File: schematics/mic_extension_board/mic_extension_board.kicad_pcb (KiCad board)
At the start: 2 copper layers, 87 x 62.2 mm, 126 parts, among them J1 XLR3, J12 Conn_01x01_Female, J13 Conn_01x01_Female, J2 Conn_01x02_Male, J3 Aux In, J4 Conn_01x02_Pin, J5 6Pin ISP, J7 XLR3, J8 XLR3, J9 Conn_01x03_Female, SW1 Stompbutton 1, SW2 Stompbutton 2, SW3 Stompbutton 3, U1 TL074, U10 LM4881M/NOPB, U11 CS4270-CZZ, U2 TL072, U3 k7833, U4 NE5534, U5 ATmega88A-A, U6 24LC128, U7 MC78M09_TO252, U8 MC78M05_TO252, U9 TL072, X1 SG-5032CAN

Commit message: finished full board
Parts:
- added C38: C, Capacitor_SMD:C_0805_2012Metric_Pad1.18x1.45mm_HandSolder, F.Cu at (187.9, 84.0)
- added C39: C, Capacitor_SMD:C_0805_2012Metric_Pad1.18x1.45mm_HandSolder, F.Cu at (187.9, 89.0)
- added D1: LED, Connector_PinHeader_2.54mm:PinHeader_1x02_P2.54mm_Vertical, F.Cu at (155.5, 124.6)
- added D8: LED, Connector_PinHeader_2.54mm:PinHeader_1x02_P2.54mm_Vertical, F.Cu at (151.0, 124.6)
- added J6: Conn_01x03_Female, Connector_PinHeader_2.54mm:PinHeader_1x03_P2.54mm_Vertical, F.Cu at (159.9, 66.2)
- added R50: R, Resistor_SMD:R_0603_1608Metric_Pad0.98x0.95mm_HandSolder, F.Cu at (194.8, 84.0)
- added R51: R, Resistor_SMD:R_0603_1608Metric_Pad0.98x0.95mm_HandSolder, F.Cu at (191.7, 84.0)
- added R52: R, Resistor_SMD:R_0603_1608Metric_Pad0.98x0.95mm_HandSolder, F.Cu at (194.8, 89.0)
- added R53: R, Resistor_SMD:R_0603_1608Metric_Pad0.98x0.95mm_HandSolder, F.Cu at (191.7, 89.0)
- added R54: 180, Resistor_SMD:R_0603_1608Metric_Pad0.98x0.95mm_HandSolder, F.Cu at (158.7, 125.9)
- added R55: 180, Resistor_SMD:R_0603_1608Metric_Pad0.98x0.95mm_HandSolder, F.Cu at (147.9, 125.9)
- added RV3: 25k, Connector_PinHeader_2.54mm:PinHeader_1x03_P2.54mm_Vertical, F.Cu at (175.8, 128.4)
- added RV4: 25k, Connector_PinHeader_2.54mm:PinHeader_1x03_P2.54mm_Vertical, F.Cu at (180.9, 128.4)
- added RV5: 25k, Connector_PinHeader_2.54mm:PinHeader_1x03_P2.54mm_Vertical, F.Cu at (185.3, 128.4)
- added SW4: Enter, Connector_PinHeader_2.54mm:PinHeader_1x02_P2.54mm_Vertical, F.Cu at (170.1, 124.6)
- added SW5: Exit, Connector_PinHeader_2.54mm:PinHeader_1x02_P2.54mm_Vertical, F.Cu at (163.1, 124.6)
- added U12: 128X64 OLED Display, Connector_PinHeader_2.54mm:PinHeader_1x07_P2.54mm_Vertical, F.Cu at (140.2, 132.2)
- added U13: Debug Port, Connector_PinHeader_2.54mm:PinHeader_1x06_P2.54mm_Vertical, F.Cu at (182.2, 132.8)
- C1: value 33pF -> C; footprint Capacitor_SMD:C_0603_1608Metric_Pad1.08x0.95mm_HandSolder -> Capacitor_SMD:C_0805_2012Metric_Pad1.18x1.45mm_HandSolder
- C10, C21, C22: value 4.7uF -> C_Polarized
- C11, C12: value 330uF -> C_Polarized
- C13, C15, C17, C23, C25, C3, C33: value 10uF -> C_Polarized
- C14, C5, C6: value 22uF -> C_Polarized
- C16, C24, C26, C31, C34, C35: value 0.1uF -> C
- C18, C27, C28: value 220pF -> C
- C19, C2, C20, C7, C8, C9: value 1uF -> C_Polarized
- C29, C30: value 3.3uF -> C_Polarized
- C32: value 47uF -> C_Polarized
- C36, C37: value 3.3nF -> C
- C4: value 47pF -> C
- J5: value 6Pin ISP -> Conn_02x03_Odd_Even
- J9: value Conn_01x03_Female -> Conn_01x03
- L1: value 22uH -> L
- R1, R15, R16, R18, R2, R29, R3, R4: value 22k -> R
- R10, R17, R19, R21, R22, R24, R25, R26, R27, R28, R31, R34, R35, R46, R47, R9: value 10k -> R
- R11, R12, R13, R14, R7, R8: value 180 -> R
- R20, R23, R42, R5: value 4k7 -> R
- R30, R32, R33, R6: value 150 -> R
- R36, R37, R38, R39: value 12k -> R
- R40: value 1M -> R
- R41, R44, R45: value 2k2 -> R
- R43: value 47k -> R
- R48, R49: value 470 -> R
- RV1: value 100k -> R_Potentiometer
- RV2: value 10k -> R_Potentiometer
- SW1: value Stompbutton 1 -> SW_Push
- SW2: value Stompbutton 2 -> SW_Push
- SW3: value Stompbutton 3 -> SW_Push
- U2: value TL072 -> Pico; footprint Package_SO:SOIC-8_3.9x4.9mm_P1.27mm -> MCU_RaspberryPi_and_Boards:RPi_Pico_SMD_TH
- U3: value k7833 -> LM7809_TO220; footprint Connector_PinHeader_2.54mm:PinHeader_1x03_P2.54mm_Vertical -> Package_TO_SOT_THT:TO-220-3_Vertical
- U7: value MC78M09_TO252 -> MC78M05_TO252
- U9: value TL072 -> TL074; footprint Package_SO:SOIC-8_3.9x4.9mm_P1.27mm -> Package_SO:SOIC-14_3.9x8.7mm_P1.27mm
- moved U2 106.4 mm to (175.2, 106.2), turned to -90 degrees
- moved J9 104.6 mm to (198.0, 88.4), turned to 180 degrees
- moved H1 94.0 mm to (196.8, 131.6)
- moved R45 84.0 mm to (87.9, 105.7), turned to 180 degrees
- moved J7 81.5 mm to (140.2, 66.2), turned to -90 degrees
- moved C25 81.2 mm to (112.3, 74.4), turned to 90 degrees
- moved R27 79.8 mm to (132.0, 88.4)
- moved R30 79.5 mm to (139.2, 68.7), turned to 180 degrees
- moved R26 78.9 mm to (131.3, 82.0)
- moved R43 78.6 mm to (112.4, 84.3), turned to 180 degrees
- moved R44 78.4 mm to (88.7, 108.7), turned to 180 degrees
- moved C23 78.3 mm to (107.9, 90.3), turned to 90 degrees
- moved R18 77.9 mm to (146.3, 80.8)
- moved J13 77.6 mm to (110.9, 95.0)
- moved R19 77.1 mm to (135.4, 85.9)
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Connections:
- C11 pad 2: Net-(J9-Pin_2) -> Net-(J6-Pin_2)
- C12 pad 2: Net-(J9-Pin_3) -> Net-(J6-Pin_3)
- C16 pad 1: Net-(U1B-+) -> Net-(U1D-+)
- C18 pad 1: Net-(U9B--) -> Net-(U1B--)
- C19 pad 1: Net-(U9B-+) -> Net-(U1B-+)
- C24 pad 1: Net-(U11-VD) -> 3V3
- C26 pad 1: Net-(U11-VD) -> 3V3
- C8 pad 1: Net-(U9A-+) -> Net-(C8-Pad1)
- J9 pad 1: GND -> Net-(J9-Pin_1)
- J9 pad 2: Net-(J9-Pin_2) -> GND
- R19 pad 2: Net-(U1D--) -> Net-(U9D--)
- R20 pad 2: Net-(U1D--) -> Net-(U9D--)
- R21 pad 2: Net-(U1C--) -> Net-(U9C--)
- R22 pad 2: Net-(U2A--) -> Net-(U9A--)
- R23 pad 2: Net-(U2A--) -> Net-(U9A--)
- R24 pad 1: Net-(U2A--) -> Net-(U9A--)
- R25 pad 2: Net-(U2B--) -> Net-(U9B--)
- R26 pad 1: Net-(U1D--) -> Net-(U9D--)
- R27 pad 1: Net-(U1C--) -> Net-(U9C--)
- R28 pad 1: Net-(U2B--) -> Net-(U9B--)
- R36 pad 2: Net-(U1B-+) -> Net-(U1D-+)
- R37 pad 1: Net-(U1B-+) -> Net-(U1D-+)
- R38 pad 2: Net-(U9A-+) -> Net-(C8-Pad1)
- R39 pad 1: Net-(U9A-+) -> Net-(C8-Pad1)
- R40 pad 1: Net-(U9A--) -> Net-(C8-Pad1)
- R40 pad 2: Net-(U9B-+) -> Net-(U1B-+)
- R41 pad 1: Net-(U9B--) -> Net-(U1B--)
- R42 pad 1: Net-(U9B--) -> Net-(U1B--)
- R44 pad 2: Net-(U11-VD) -> 3V3
- R45 pad 2: Net-(U11-VD) -> 3V3
- U1 pad 10: VGND -> GND
- U1 pad 12: VGND -> Net-(U1D-+)
- U1 pad 13: Net-(U1D--) -> VGND
- U1 pad 14: Net-(C3-Pad1) -> VGND
- U1 pad 6: VGND -> Net-(U1B--)
- U1 pad 7: VGND -> Net-(C18-Pad2)
- U1 pad 8: Net-(C13-Pad1) -> Net-(U1C--)
- U11 pad 5: Net-(U11-VD) -> 3V3
- U11 pad 8: Net-(U11-VD) -> 3V3
- U2 pad 1: /Analog Preamp/Left Analog Out -> Net-(U13-UartTX)
- U2 pad 2: Net-(U2A--) -> Net-(U13-UartRX)
- U2 pad 3: VGND -> GND
- U2 pad 4: GND -> unconnected-(U2-GPIO2-Pad4)
- U2 pad 5: VGND -> /Codec/codec_reset
- U2 pad 6: Net-(U2B--) -> /Codec/SDA
- U2 pad 7: Net-(C15-Pad1) -> /Codec/SCL
- U2 pad 8: +9V -> GND
- U9 pad 1: Net-(U9A--) -> /Analog Preamp/Left Analog Out
- U9 pad 3: Net-(U9A-+) -> VGND
- U9 pad 4: GND -> +9V
- U9 pad 5: Net-(U9B-+) -> VGND
- U9 pad 7: Net-(C18-Pad2) -> Net-(C15-Pad1)
- U9 pad 8: +9V -> Net-(C13-Pad1)
- X1 pad 4: Net-(U11-VD) -> 3V3
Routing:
- net GND: track 98.8 -> 261.4 mm, vias 15 -> 25
- net 5V: track 65.2 -> 194.0 mm, vias 2 -> 5
- net /Codec/SCL: track 11.6 -> 116.6 mm, vias 0 -> 2
- net /Codec/SDA: track 11.6 -> 114.7 mm
- net Net-(U12-3.3V): track 0.00 -> 95.3 mm, vias 0 -> 5
- net /Codec/codec_reset: track 0.00 -> 94.5 mm, vias 0 -> 5
- net 3V3: track 27.8 -> 114.7 mm
- net /Codec/codec_lrckl: track 0.00 -> 75.0 mm, vias 0 -> 2
- net /Codec/codec_sdin: track 0.00 -> 71.9 mm, vias 0 -> 2
- net /Codec/codec_sdout: track 0.00 -> 70.1 mm, vias 0 -> 2
- net /Codec/codec_sclk: track 0.00 -> 68.2 mm, vias 0 -> 2
- net Net-(U12-DC): track 0.00 -> 51.2 mm, vias 0 -> 2
- net Net-(U13-SWCLK): track 0.00 -> 49.3 mm, vias 0 -> 2
- net Net-(U13-SWDIO): track 0.00 -> 47.5 mm
- net Net-(U13-UartRX): track 0.00 -> 47.2 mm, vias 0 -> 2
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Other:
- board size 87 x 62.2 mm -> 127 x 73 mm
- board text added: "12V In"
- board text added: "HiZ"
- board text added: "Vol HiZ"
- board text added: "Vol mic."
- board text removed: "AC In"
- board text removed: "AdcIn"
- board text removed: "DacL"
- board text removed: "DacR"
- board text removed: "I2C"
- board text removed: "SCL"
- board text removed: "SDA"
- board text removed: "Vol."

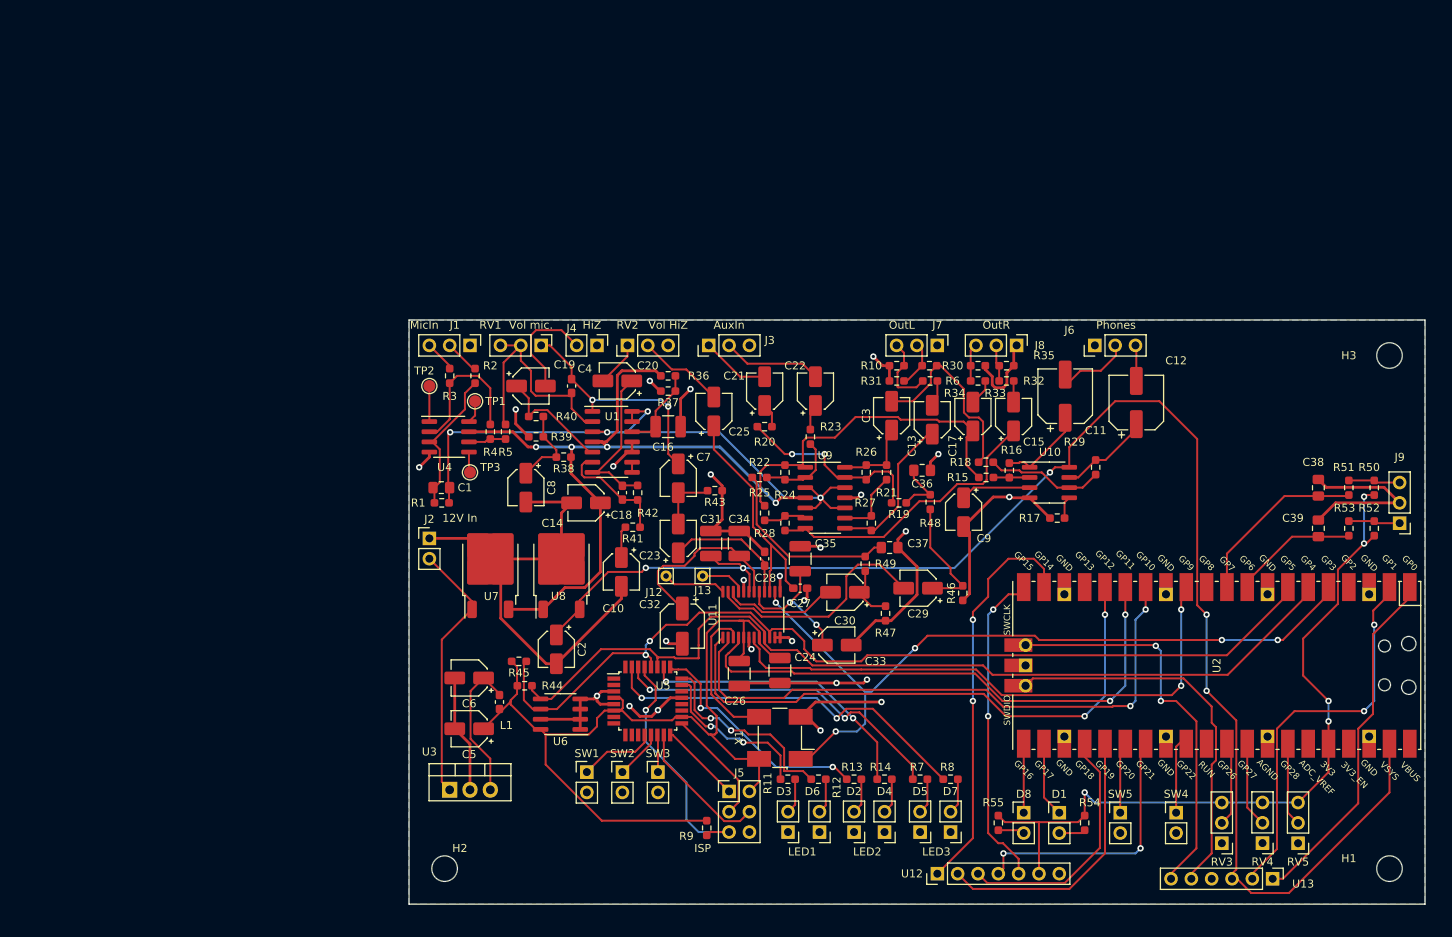
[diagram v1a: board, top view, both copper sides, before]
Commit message: re-added component values previously lost due to kicad mishap
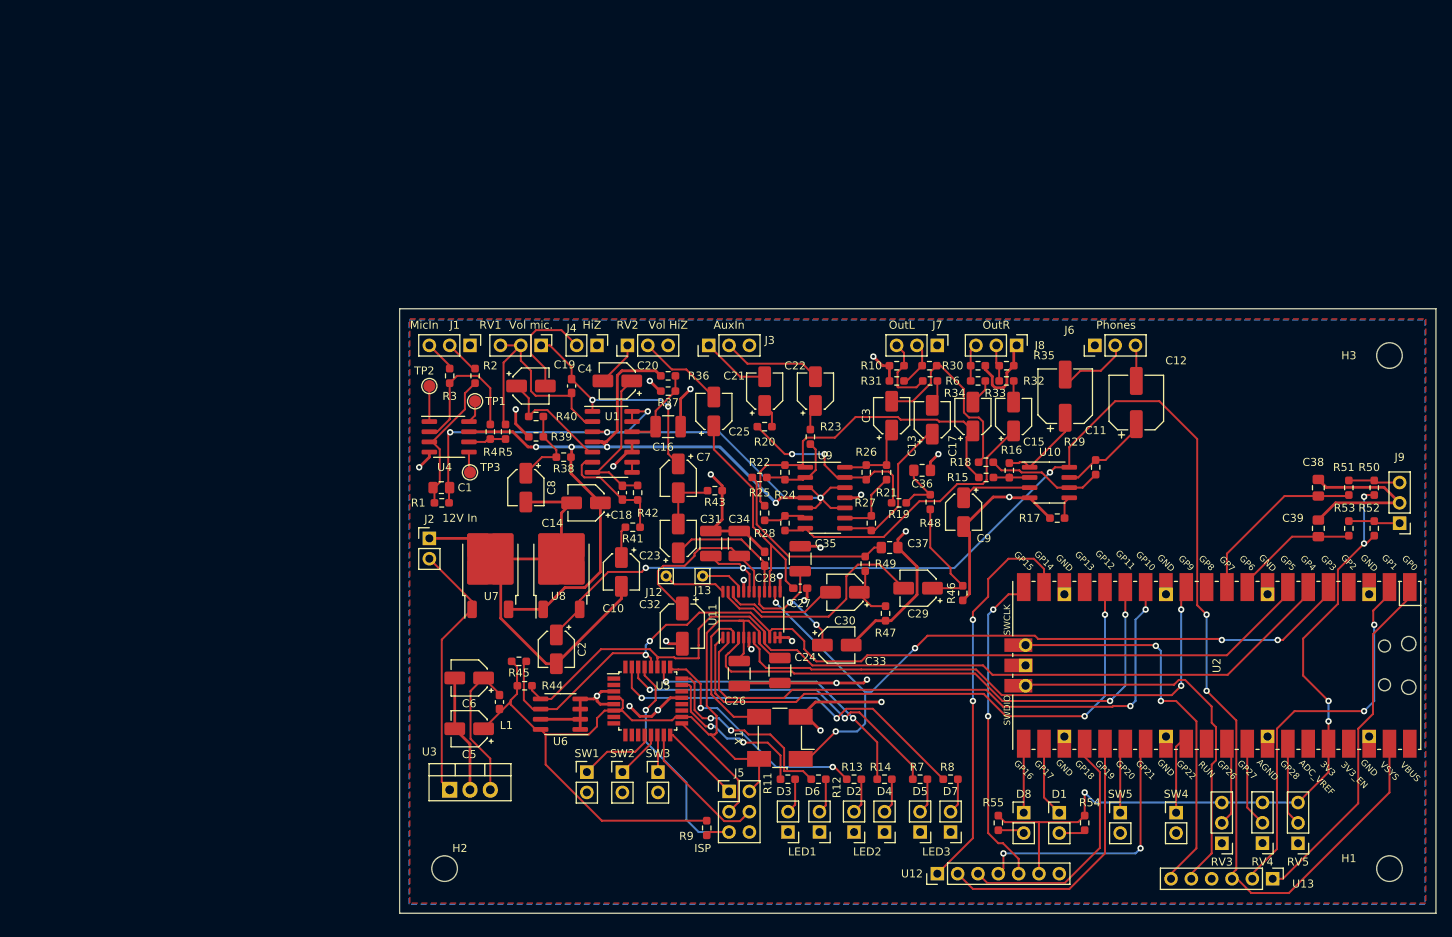
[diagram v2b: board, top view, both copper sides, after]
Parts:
- C1: value C -> 33pF
- C10, C21, C22: value C_Polarized -> 4.7uF
- C11, C12: value C_Polarized -> 330uF
- C13, C15, C17, C23, C25, C3, C33: value C_Polarized -> 10uF
- C14, C5, C6: value C_Polarized -> 22uF
- C16, C24, C26, C31, C34, C35: value C -> 0.1uF
- C18, C27, C28: value C -> 220pF
- C19, C2, C20, C7, C8, C9: value C_Polarized -> 1uF
- C29, C30: value C_Polarized -> 3.3uF
- C32: value C_Polarized -> 47uF
- C36, C37: value C -> 3.3nF
- C38, C39: value C -> 0.01uF
- C4: value C -> 47pF
- L1: value L -> 22uH
- R1, R15, R16, R18, R2, R29, R3, R4: value R -> 22k
- R10, R17, R19, R21, R22, R24, R25, R26, R27, R28, R31, R34, R35, R46, R47, R50, R51, R52, R53, R9: value R -> 10k
- R11, R12, R13, R14, R7, R8: value R -> 180
- R20, R23, R42, R5: value R -> 4k7
- R30, R32, R33, R6: value R -> 150
- R36, R37, R38, R39: value R -> 12k
- R40: value R -> 1M
- R41, R44, R45: value R -> 2k2
- R43: value R -> 47k
- R48, R49: value R -> 470
- RV1: value R_Potentiometer -> 100k
- RV2: value R_Potentiometer -> 10k
- SW1: value SW_Push -> Stompbutton 1
- SW2: value SW_Push -> Stompbutton 2
- SW3: value SW_Push -> Stompbutton 3
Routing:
- added copper zone on F.Cu, net 5V
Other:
- board size 127 x 73 mm -> 129.5 x 75.6 mm

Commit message: schematic / pcb update
* digital part is now driven from 3.3v only
* 3.3v switching supply is now present as discrete parts
* top copper fill is 3.3v
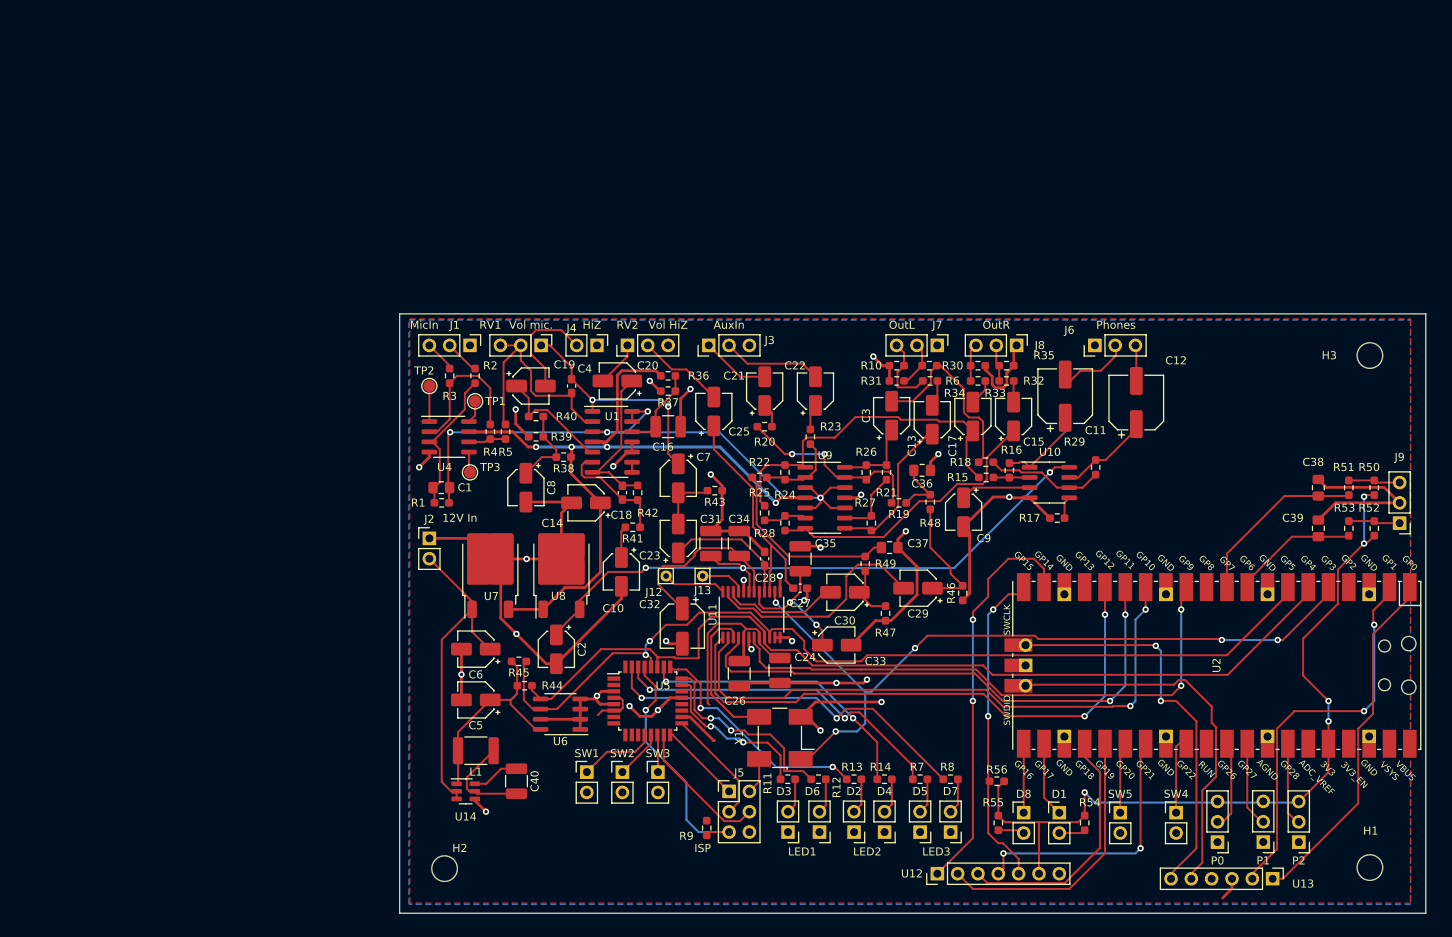
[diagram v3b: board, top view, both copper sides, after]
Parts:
- removed RV3, RV4, RV5: 25k, Connector_PinHeader_2.54mm:PinHeader_1x03_P2.54mm_Vertical
- removed U3: LM7809_TO220, Package_TO_SOT_THT:TO-220-3_Vertical
- added C40: 0.1uF, Capacitor_SMD:C_1210_3225Metric_Pad1.33x2.70mm_HandSolder, F.Cu at (87.6, 120.7)
- added P0: 25k, Connector_PinHeader_2.54mm:PinHeader_1x03_P2.54mm_Vertical, F.Cu at (175.3, 128.3)
- added P1: 25k, Connector_PinHeader_2.54mm:PinHeader_1x03_P2.54mm_Vertical, F.Cu at (181.0, 128.3)
- added P2: 25k, Connector_PinHeader_2.54mm:PinHeader_1x03_P2.54mm_Vertical, F.Cu at (185.4, 128.3)
- added R56: 10k, Resistor_SMD:R_0603_1608Metric_Pad0.98x0.95mm_HandSolder, F.Cu at (147.7, 120.7)
- added U14: AP63203WU, Package_TO_SOT_SMD:TSOT-23-6, F.Cu at (81.3, 121.9)
- C6: value 22uF -> 10uF
- L1: value 22uH -> 3.9uH; footprint Inductor_SMD:L_0603_1608Metric_Pad1.05x0.95mm_HandSolder -> Inductor_SMD:L_1812_4532Metric_Pad1.30x3.40mm_HandSolder
- moved L1 6.77 mm to (82.5, 116.8), turned to 180 degrees
- moved C5 3.70 mm to (82.5, 110.5)
- moved C6 3.70 mm to (82.5, 104.1)
- moved H1 2.45 mm to (194.3, 131.4)
- moved H3 2.44 mm to (194.3, 67.4)
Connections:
- C6 pad 1: Net-(U3-VO) -> Net-(J2-Pin_2)
- L1 pad 1: Net-(U3-VO) -> Net-(U14-SW)
- U13 pad 3: 5V -> 3V3
- U2 pad 39: 5V -> 3V3
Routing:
- net 5V: track 194.0 -> 81.7 mm, vias 5 -> 3
- net 3V3: track 114.7 -> 70.9 mm
- net Net-(U3-VO): track 18.6 -> 0.00 mm
- net Net-(U14-SW): track 0.00 -> 12.6 mm
- net Net-(J2-Pin_2): track 33.1 -> 40.8 mm
- net GND: track 261.4 -> 255.2 mm, vias 25 -> 29
- net Net-(U14-BST): track 0.00 -> 5.99 mm
- net Net-(U12-3.3V): track 95.3 -> 99.9 mm
- added copper zone on F.Cu, net 3V3
- removed copper zone on F.Cu, net 5V
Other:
- board size 129.5 x 75.6 mm -> 128.3 x 74.9 mm

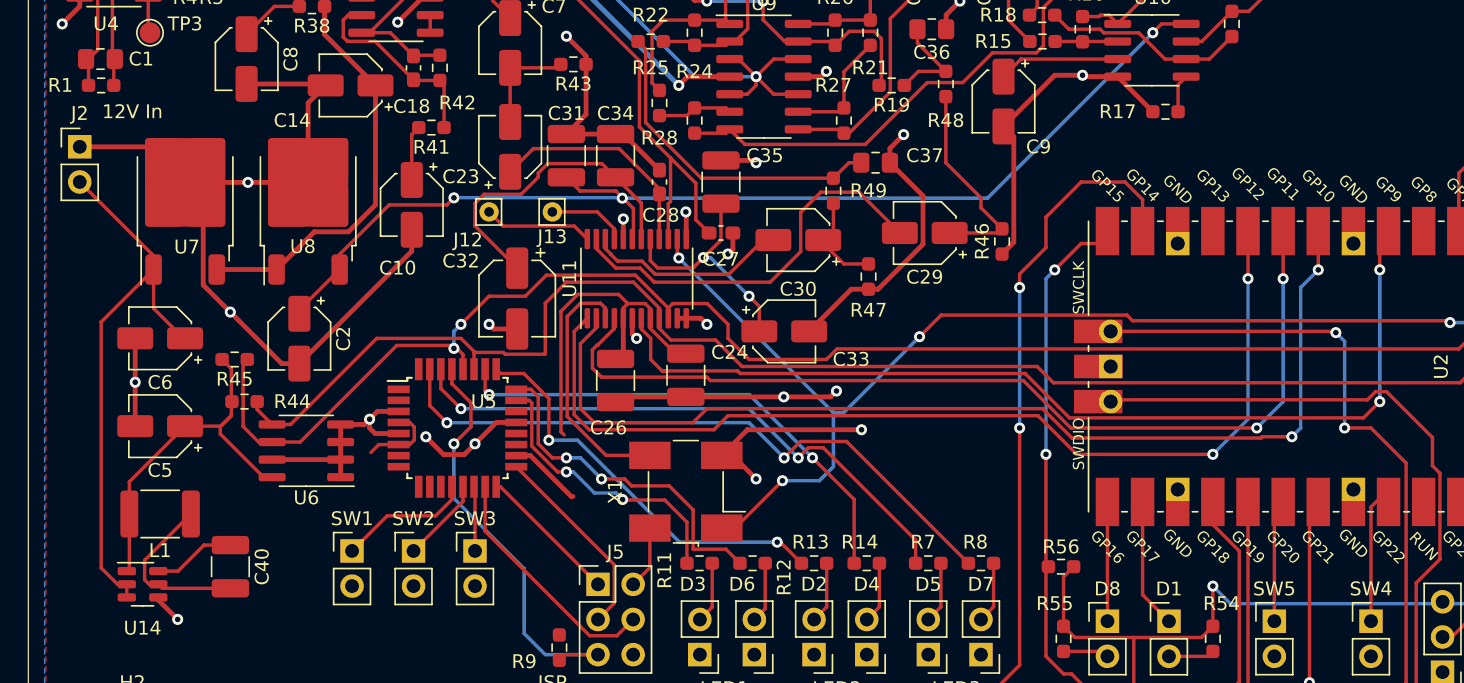
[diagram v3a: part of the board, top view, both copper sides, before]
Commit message: schematics
adjusted track widths
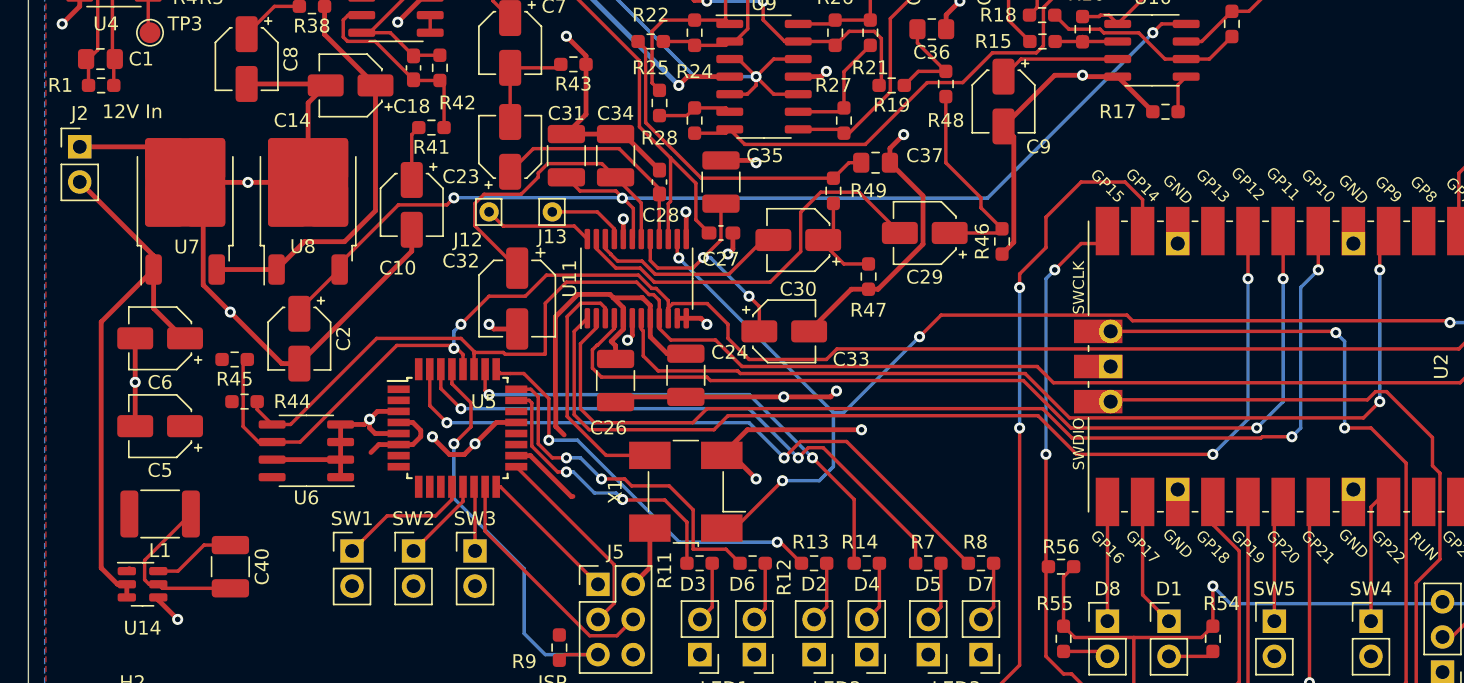
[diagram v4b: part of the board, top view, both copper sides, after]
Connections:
- net Net-(J2-Pin_2) renamed Vin
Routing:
- net 3V3: track 70.9 -> 47.2 mm
